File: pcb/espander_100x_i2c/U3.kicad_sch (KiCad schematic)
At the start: 5 parts, among them J1 DG127A-5.08-06P-14-00AH, J2 DG127A-5.08-06P-14-00AH, J3 DG127A-5.08-06P-14-00AH, J4 DG127A-5.08-06P-14-00AH, U1 MCP23017_SP

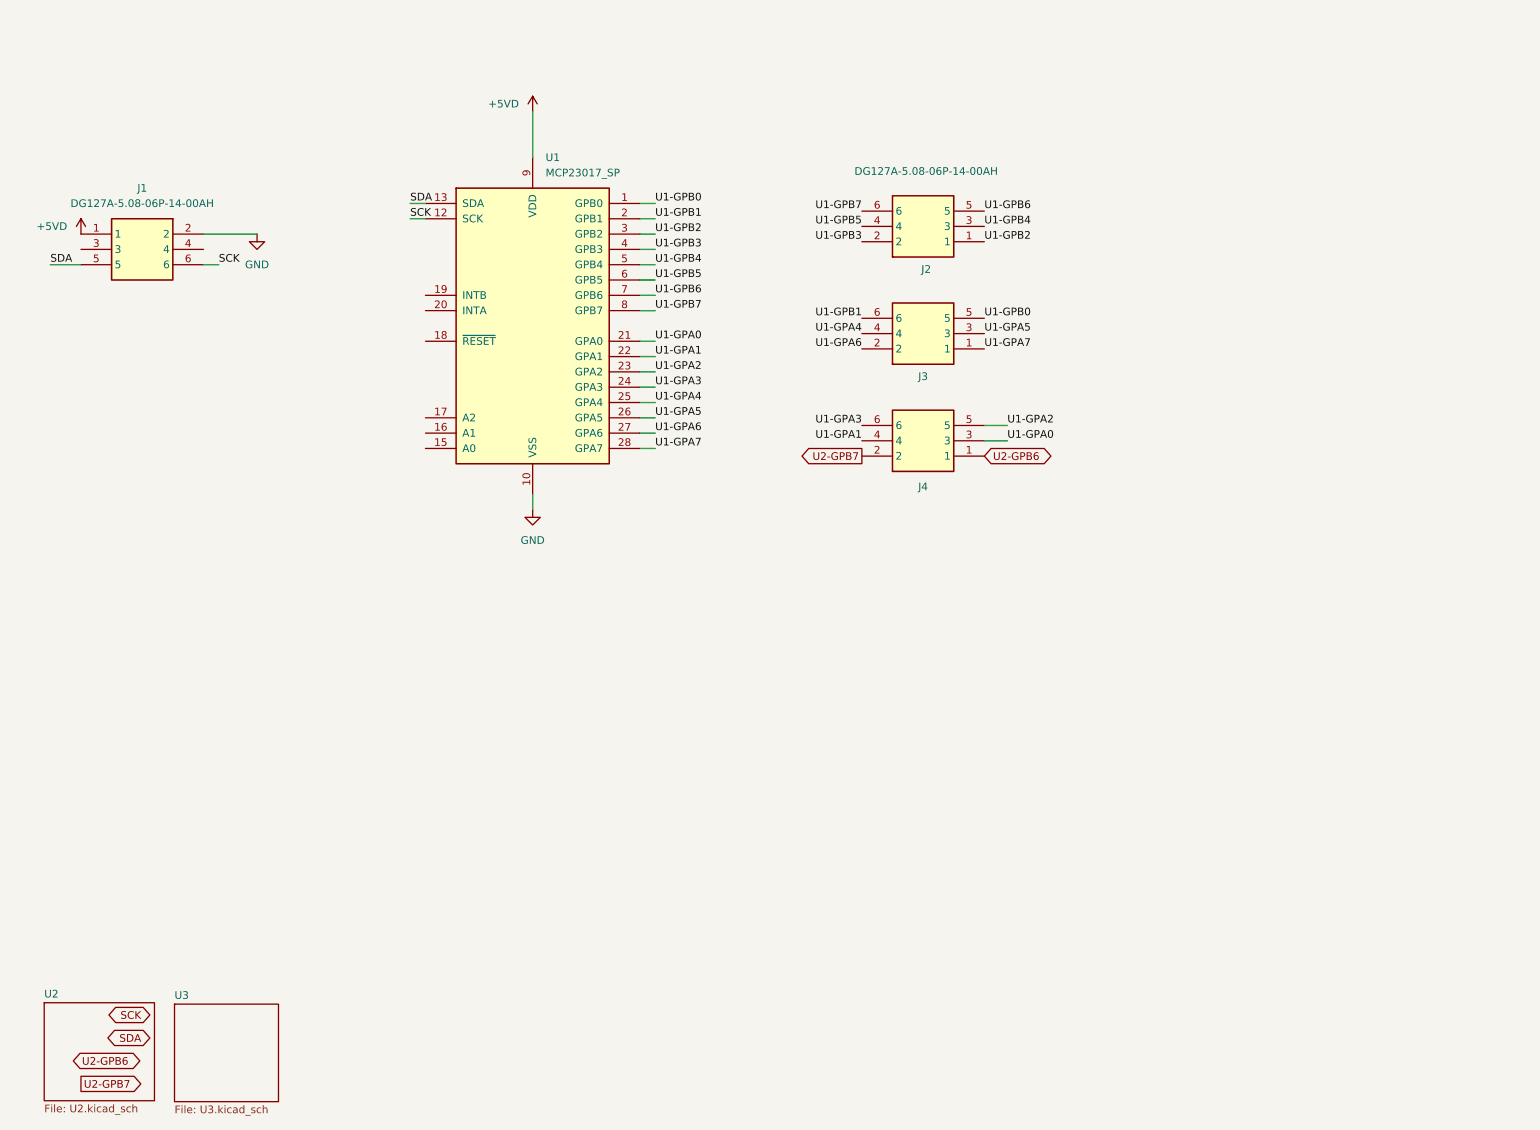
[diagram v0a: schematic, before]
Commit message: Add initial DRU file for espander_100x_i2c PCB design
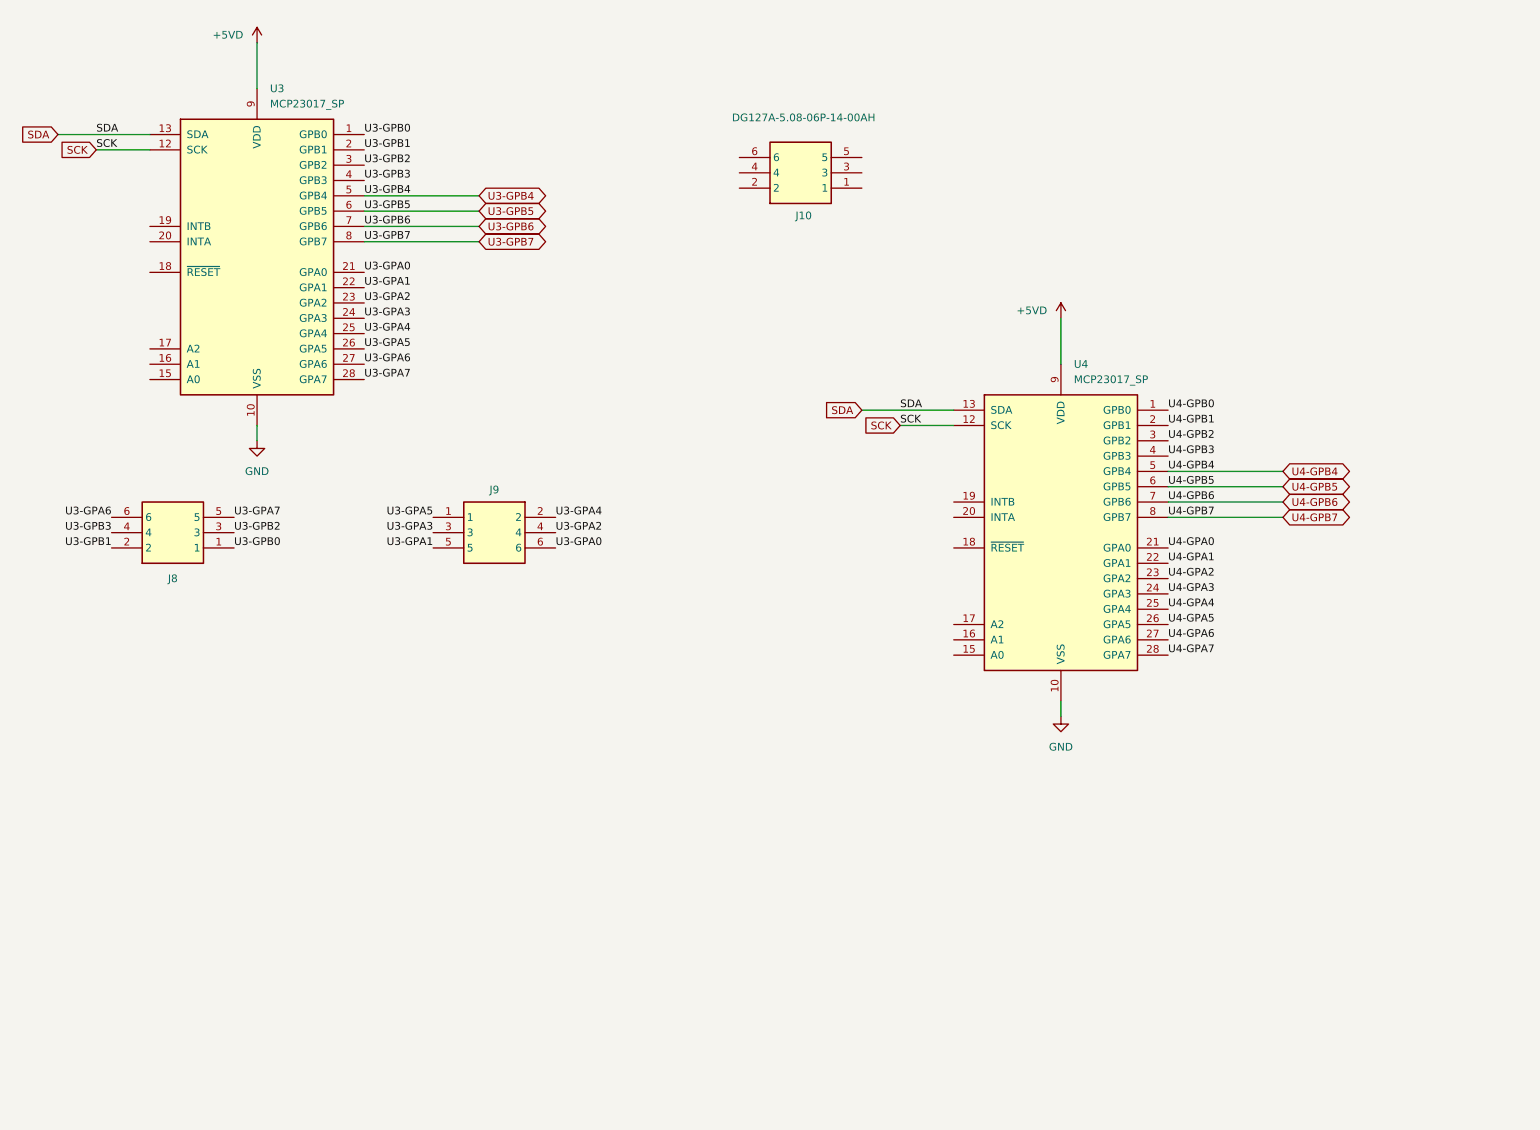
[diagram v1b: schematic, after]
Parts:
- removed J1, J2, J3, J4: DG127A-5.08-06P-14-00AH, DG127A50806P1400AH, symbol 1_tme:DG127A-5.08-06P-14-00AH
- removed U1: MCP23017_SP, Package_DIP:DIP-28_W7.62mm, symbol Interface_Expansion:MCP23017_SP
- added J10, J8, J9: DG127A-5.08-06P-14-00AH, DG127A50806P1400AH, symbol 1_tme:DG127A-5.08-06P-14-00AH
- added U3, U4: MCP23017_SP, Package_DIP:DIP-28_W7.62mm, symbol Interface_Expansion:MCP23017_SP
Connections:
- net +5VD: now also U3.9 (VDD), U4.9 (VDD)
- net GND: now also U3.10 (VSS), U4.10 (VSS)
- net SCK: now also U3.12 (SCK), U4.12 (SCK)
- net SDA: now also U3.13 (SDA), U4.13 (SDA)
- new net U3-GPA0: J9.6, U3.21 (GPA0)
- new net U3-GPA1: J9.5, U3.22 (GPA1)
- new net U3-GPA2: J9.4, U3.23 (GPA2)
- new net U3-GPA3: J9.3, U3.24 (GPA3)
- new net U3-GPA4: J9.2, U3.25 (GPA4)
- new net U3-GPA5: J9.1, U3.26 (GPA5)
- new net U3-GPA6: J8.6, U3.27 (GPA6)
- new net U3-GPA7: J8.5, U3.28 (GPA7)
- new net U3-GPB0: J8.1, U3.1 (GPB0)
- new net U3-GPB1: J8.2, U3.2 (GPB1)
- new net U3-GPB2: J8.3, U3.3 (GPB2)
- new net U3-GPB3: J8.4, U3.4 (GPB3)
- new net U3-GPB4: U3.5 (GPB4)
- new net U3-GPB5: U3.6 (GPB5)
- new net U3-GPB6: U3.7 (GPB6)
- new net U3-GPB7: U3.8 (GPB7)
- new net U4-GPA0: U4.21 (GPA0)
- new net U4-GPA1: U4.22 (GPA1)
- new net U4-GPA2: U4.23 (GPA2)
- new net U4-GPA3: U4.24 (GPA3)
- new net U4-GPA4: U4.25 (GPA4)
- new net U4-GPA5: U4.26 (GPA5)
- new net U4-GPA6: U4.27 (GPA6)
- new net U4-GPA7: U4.28 (GPA7)
- new net U4-GPB0: U4.1 (GPB0)
- new net U4-GPB1: U4.2 (GPB1)
- new net U4-GPB2: U4.3 (GPB2)
- new net U4-GPB3: U4.4 (GPB3)
- new net U4-GPB4: U4.5 (GPB4)
- new net U4-GPB5: U4.6 (GPB5)
- new net U4-GPB6: U4.7 (GPB6)
- new net U4-GPB7: U4.8 (GPB7)
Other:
- removed sheet U2
- removed sheet U3

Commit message: Refactor code structure for improved readability and maintainability
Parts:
- added J11: DG127A-5.08-06P-14-00AH, DG127A50806P1400AH, symbol 1_tme:DG127A-5.08-06P-14-00AH
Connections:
- net U3-GPA0: no longer J9.6
- net U3-GPA1: no longer J9.5
- net U3-GPA2: no longer J9.4
- net U3-GPA3: no longer J9.3
- net U3-GPA4: no longer J9.2
- net U3-GPA5: no longer J9.1
- net U3-GPA6: no longer J8.6
- net U3-GPA7: no longer J8.5
- net U3-GPB0: no longer J8.1
- net U3-GPB1: no longer J8.2
- net U3-GPB2: no longer J8.3
- net U3-GPB3: no longer J8.4
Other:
- moved on the sheet: J10, U4

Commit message: RESYNC
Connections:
- net U3-GPA0: now also J9.1
- net U3-GPA1: now also J9.2
- net U3-GPA2: now also J9.3
- net U3-GPA3: now also J9.4
- net U3-GPA4: now also J9.5
- net U3-GPA5: now also J9.6
- net U3-GPA6: now also J8.2
- net U3-GPA7: now also J8.1
- net U3-GPB0: now also J8.3
- net U3-GPB1: now also J8.4
- net U3-GPB2: now also J8.5
- net U3-GPB3: now also J8.6
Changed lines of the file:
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@@
 	(generator_version "9.0")
 	(paper "A4")
-	(text_box "U3 - J8 - J9"
-		(exclude_from_sim no)
-		(at 12.7 13.97 0)
-		(size 110.49 101.6)
-		(margins 0.9525 0.9525 0.9525 0.9525)
-		(stroke
-			(width 0)
-			(type solid)
-		)
-		(fill
-			(type color)
-			(color 135 217 255 0.21)
-		)
-		(effects
-			(font
-				(size 1.27 1.27)
-				(thickness 0.254)
-				(bold yes)
-			)
-			(justify left top)
-		)
-	)
 	(wire
 		(pts
@@
 		)
 	)
+	(label "U3-GPA3"
+		(at 102.87 100.33 0)
+		(effects
+			(font
+				(size 1.27 1.27)
+			)
+			(justify left bottom)
+		)
+		(property "Netclass" "GPIO"
+			(at 112.776 100.33 0)
+			(effects
+				(font
+					(size 1.27 1.27)
+					(italic yes)
+				)
+				(justify left)
+			)
+		)
+	)
 	(label "U4-GPB4"
 		(at 187.96 45.72 0)
@@
 		)
 	)
+	(label "U3-GPA2"
+		(at 82.55 100.33 180)
+		(effects
+			(font
+				(size 1.27 1.27)
+			)
+			(justify right bottom)
+		)
+		(property "Netclass" "GPIO"
+			(at 72.644 100.33 0)
+			(effects
+				(font
+					(size 1.27 1.27)
+					(italic yes)
+				)
+				(justify right)
+			)
+		)
+	)
+	(label "U3-GPA4"
+		(at 82.55 102.87 180)
+		(effects
+			(font
+				(size 1.27 1.27)
+			)
+			(justify right bottom)
+		)
+		(property "Netclass" "GPIO"
+			(at 72.644 102.87 0)
+			(effects
+				(font
+					(size 1.27 1.27)
+					(italic yes)
+				)
+				(justify right)
+			)
+		)
+	)
 	(label "U3-GPB6"
 		(at 71.12 49.53 0)
@@
 		)
 	)
+	(label "U3-GPB1"
+		(at 29.21 100.33 180)
+		(effects
+			(font
+				(size 1.27 1.27)
+			)
+			(justify right bottom)
+		)
+		(property "Netclass" "GPIO"
+			(at 19.304 100.33 0)
+			(effects
+				(font
+					(size 1.27 1.27)
+					(italic yes)
+				)
+				(justify right)
+			)
+		)
+	)
+	(label "U3-GPA7"
+		(at 49.53 102.87 0)
+		(effects
+			(font
+				(size 1.27 1.27)
+			)
+			(justify left bottom)
+		)
+		(property "Netclass" "GPIO"
+			(at 59.436 102.87 0)
+			(effects
+				(font
+					(size 1.27 1.27)
+					(italic yes)
+				)
+				(justify left)
+			)
+		)
+	)
 	(label "U3-GPB2"
 		(at 71.12 39.37 0)
@@
 		)
 	)
+	(label "U3-GPB0"
+		(at 49.53 100.33 0)
+		(effects
+			(font
+				(size 1.27 1.27)
+			)
+			(justify left bottom)
+		)
+		(property "Netclass" "GPIO"
+			(at 59.436 100.33 0)
+			(effects
+				(font
+					(size 1.27 1.27)
+					(italic yes)
+				)
+				(justify left)
+			)
+		)
+	)
 	(label "U4-GPB0"
 		(at 187.96 35.56 0)
@@
 		)
 	)
+	(label "U3-GPA5"
+		(at 102.87 102.87 0)
+		(effects
+			(font
+				(size 1.27 1.27)
+			)
+			(justify left bottom)
+		)
+		(property "Netclass" "GPIO"
+			(at 112.776 102.87 0)
+			(effects
+				(font
+					(size 1.27 1.27)
+					(italic yes)
+				)
+				(justify left)
+			)
+		)
+	)
 	(label "U3-GPA4"
 		(at 71.12 67.31 0)
@@
 		)
 	)
+	(label "U3-GPA0"
+		(at 82.55 97.79 180)
+		(effects
+			(font
+				(size 1.27 1.27)
+			)
+			(justify right bottom)
+		)
+		(property "Netclass" "GPIO"
+			(at 72.39 97.79 0)
+			(effects
+				(font
+					(size 1.27 1.27)
+					(italic yes)
+				)
+				(justify right)
+			)
+		)
+	)
+	(label "U3-GPB3"
+		(at 29.21 97.79 180)
+		(effects
+			(font
+				(size 1.27 1.27)
+			)
+			(justify right bottom)
+		)
+		(property "Netclass" "GPIO"
+			(at 19.304 97.79 0)
+			(effects
+				(font
+					(size 1.27 1.27)
+					(italic yes)
+				)
+				(justify right)
+			)
+		)
+	)
+	(label "U3-GPA1"
+		(at 102.87 97.79 0)
+		(effects
+			(font
+				(size 1.27 1.27)
+			)
+			(justify left bottom)
+		)
+		(property "Netclass" "GPIO"
+			(at 113.03 97.79 0)
+			(effects
+				(font
+					(size 1.27 1.27)
+					(italic yes)
+				)
+				(justify left)
+			)
+		)
+	)
 	(label "U4-GPA3"
 		(at 187.96 66.04 0)
@@
 		)
 	)
+	(label "U3-GPB2"
+		(at 49.53 97.79 0)
+		(effects
+			(font
+				(size 1.27 1.27)
+			)
+			(justify left bottom)
+		)
+		(property "Netclass" "GPIO"
+			(at 59.436 97.79 0)
+			(effects
+				(font
+					(size 1.27 1.27)
+					(italic yes)
+				)
+				(justify left)
+			)
+		)
+	)
 	(label "U4-GPB6"
 		(at 187.96 50.8 0)
@@
 				)
 				(justify left)
+			)
+		)
+	)
+	(label "U3-GPA6"
+		(at 29.21 102.87 180)
+		(effects
+			(font
+				(size 1.27 1.27)
+			)
+			(justify right bottom)
+		)
+		(property "Netclass" "GPIO"
+			(at 19.304 102.87 0)
+			(effects
+				(font
+					(size 1.27 1.27)
+					(italic yes)
+				)
+				(justify right)
 			)
 		)
@@
 				)
 				(justify right)
-				(hide yes)
-			)
-		)
-	)
-	(global_label "U3-GPB6"
-		(shape bidirectional)
-		(at 90.17 49.53 0)
-		(fields_autoplaced yes)
-		(effects
-			(font
-				(size 1.27 1.27)
-			)
-			(justify left)
-		)
-		(property "Intersheetrefs" "${INTERSHEET_REFS}"
-			(at 103.3984 49.53 0)
-			(effects
-				(font
-					(size 1.27 1.27)
-				)
-				(justify left)
-				(hide yes)
-			)
-		)
-	)
-	(global_label "U3-GPB7"
-		(shape bidirectional)
-		(at 90.17 52.07 0)
-		(fields_autoplaced yes)
-		(effects
-			(font
-				(size 1.27 1.27)
-			)
-			(justify left)
-		)
-		(property "Intersheetrefs" "${INTERSHEET_REFS}"
-			(at 103.3984 52.07 0)
-			(effects
-				(font
-					(size 1.27 1.27)
-				)
-				(justify left)
-				(hide yes)
-			)
-		)
-	)
-	(global_label "U3-GPB5"
-		(shape bidirectional)
-		(at 90.17 46.99 0)
-		(fields_autoplaced yes)
-		(effects
-			(font
-				(size 1.27 1.27)
-			)
-			(justify left)
-		)
-		(property "Intersheetrefs" "${INTERSHEET_REFS}"
-			(at 103.3984 46.99 0)
-			(effects
-				(font
-					(size 1.27 1.27)
-				)
-				(justify left)
-				(hide yes)
-			)
-		)
-	)
-	(global_label "U3-GPB4"
-		(shape bidirectional)
-		(at 90.17 44.45 0)
-		(fields_autoplaced yes)
-		(effects
-			(font
-				(size 1.27 1.27)
-			)
-			(justify left)
-		)
-		(property "Intersheetrefs" "${INTERSHEET_REFS}"
-			(at 103.3984 44.45 0)
-			(effects
-				(font
-					(size 1.27 1.27)
-				)
-				(justify left)
 				(hide yes)
 			)
@@
 		(fields_autoplaced yes)
 		(property "Reference" "U3"
-			(at 55.4833 26.67 0)
-			(effects
-				(font
-					(size 1.27 1.27)
+			(at 55.4833 25.4 0)
+			(effects
+				(font
+					(size 2.54 2.54)
+					(thickness 0.508)
+					(bold yes)
 				)
 				(justify left)
@@
 		(fields_autoplaced yes)
 		(property "Reference" "U4"
-			(at 172.3233 27.94 0)
-			(effects
-				(font
-					(size 1.27 1.27)
-				)
-				(justify left)
+			(at 172.3233 26.67 0)
+			(effects
+				(font
+					(size 2.54 2.54)
+					(thickness 0.508)
+					(bold yes)
+				)
+				(justify left)

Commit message: Resync
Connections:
- net U4-GPA1: now also J11.6
- net U4-GPA2: now also J11.1
- net U4-GPA3: now also J11.2
- net U4-GPA4: now also J11.3
- net U4-GPA5: now also J11.4
- net U4-GPA6: now also J11.5
- net U4-GPB0: now also J10.1
- net U4-GPB1: now also J10.2
- net U4-GPB2: now also J10.3
- net U4-GPB3: now also J10.4
- net U4-GPB4: now also J10.5
- net U4-GPB5: now also J10.6

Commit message: resync
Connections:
- net U3-GPA0: no longer J9.1
- net U3-GPA1: no longer J9.2
- net U3-GPA2: no longer J9.3
- net U3-GPA3: no longer J9.4
- net U3-GPA4: no longer J9.5
- net U3-GPA5: no longer J9.6
- net U3-GPA6: no longer J8.2
- net U3-GPA7: no longer J8.1
- net U3-GPB0: no longer J8.3
- net U3-GPB1: no longer J8.4
- net U3-GPB2: no longer J8.5
- net U3-GPB3: no longer J8.6
- net U4-GPA1: no longer J11.6
- net U4-GPA2: no longer J11.1
- net U4-GPA3: no longer J11.2
- net U4-GPA4: no longer J11.3
- net U4-GPA5: no longer J11.4
- net U4-GPA6: no longer J11.5
- net U4-GPB0: no longer J10.1
- net U4-GPB1: no longer J10.2
- net U4-GPB2: no longer J10.3
- net U4-GPB3: no longer J10.4
- net U4-GPB4: no longer J10.5
- net U4-GPB5: no longer J10.6

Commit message: ekspander resync
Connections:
- net +5VD renamed +3V3
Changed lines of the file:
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@@
 			)
 		)
-		(property "Value" "+5VD"
+		(property "Value" "+3V3"
 			(at 48.514 17.78 0)
 			(effects
@@
 			)
 		)
-		(property "Value" "+5VD"
+		(property "Value" "+3V3"
 			(at 165.354 19.05 0)
 			(effects
